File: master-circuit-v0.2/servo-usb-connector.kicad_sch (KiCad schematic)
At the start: 12 parts

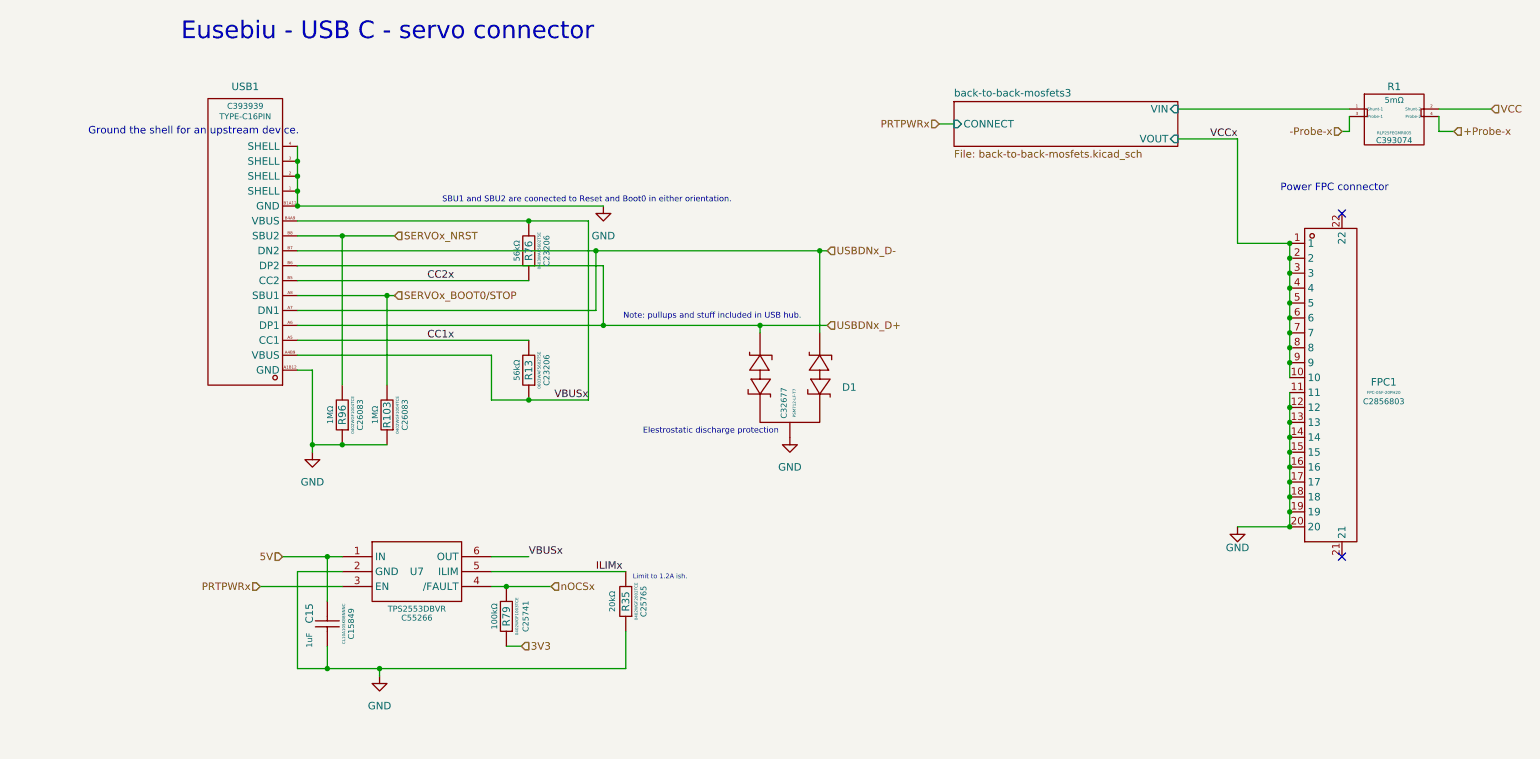
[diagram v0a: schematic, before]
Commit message: Argh, some chips out of stock, got to do a slight redesign.
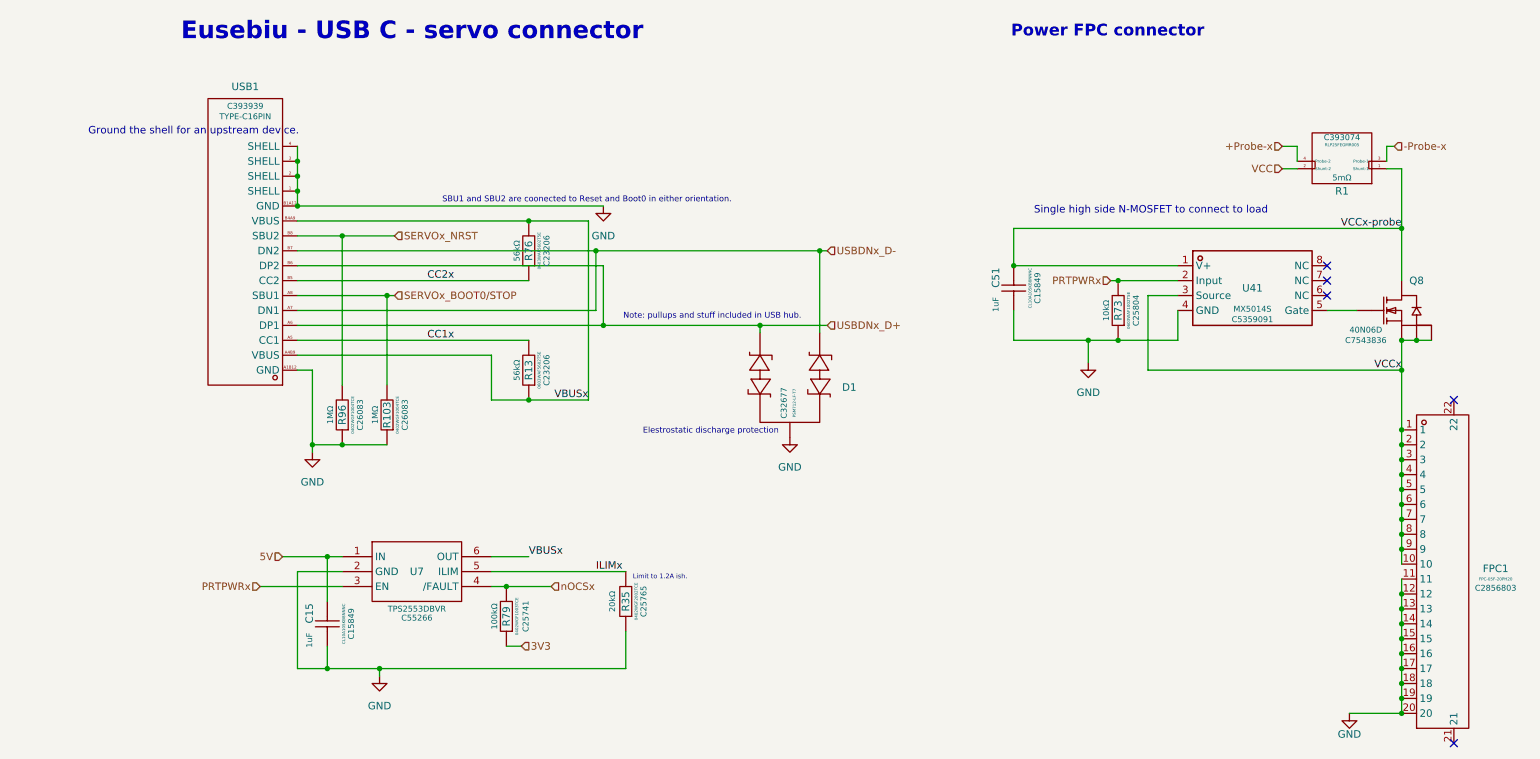
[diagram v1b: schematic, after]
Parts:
- added C51: 1uF, Library:C0603, symbol Library:CL10A105KB8NNNC Capacitor 1uF
- added Q8: (no value), Library:WDFN-5_L3.1-W3.1-P0.65-BL_1, symbol Library:40N06D MOSFET N-Channel 40A
- added R73: 10kΩ, Library:R0603, symbol Library:0603WAF1002T5E Resistor 10kΩ
- added U41: (no value), Library:SOIC-8_L4.9-W3.9-P1.27-LS6.0-BL, symbol Library:MX5014S High side/Low side MOSFET gate driver
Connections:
- net GND: now also C51.1, R73.1, U41.4 (GND)
- net PRTPWRx: now also R73.2, U41.2 (Input)
- net VCCx: now also Q8.1 (S), Q8.2 (S), Q8.3 (S), U41.3 (Source)
- net back-to-back-mosfets3/VIN renamed VCCx-probe
- net VCCx-probe: now also C51.2, Q8.5 (D), U41.1 (V+)
- new net: Q8.4 (G), U41.5 (Gate)
- no-connect marks 2 -> 5
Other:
- removed sheet back-to-back-mosfets3
- note added: "Single high side N-MOSFET to connect to load"
- moved on the sheet: FPC1
